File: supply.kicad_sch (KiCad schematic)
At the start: 95 parts, among them J12 Molex_Nano-Fit-105430_xx02-ho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, Q11 PJE138K, Q13 BCM857BS-7-F, Q14 BCM857BS-7-F, Q15 SSM3J332R, Q16 SSM3J332R, Q18 SSM3J332R, Q5 PJE138K, Q6 SSM3J332R, Q7 PJE138K, Q8 PJE138K, SW1 PCM12SMTR, U1 TPS56C230, U29 TPS56C230, U37 74LVC2G14GV, U38 74LVC1G175GV, U41 NCP730BMT330TBG, U42 TPS7A0518PDBVT

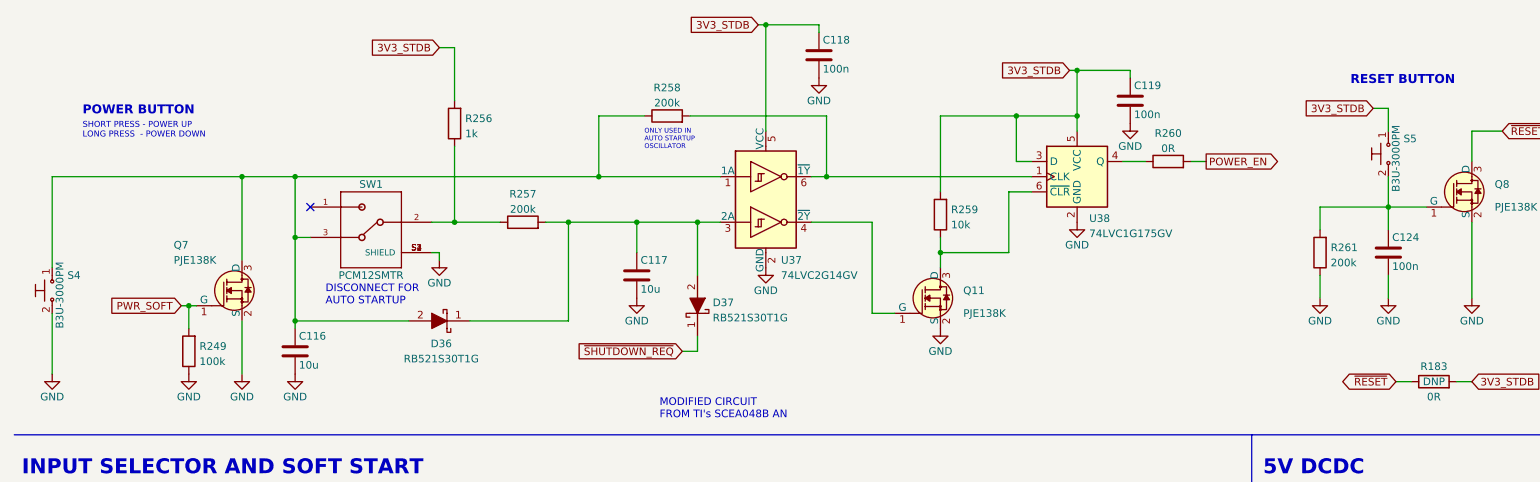
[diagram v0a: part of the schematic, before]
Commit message: Replace buttons with top-actuated ones
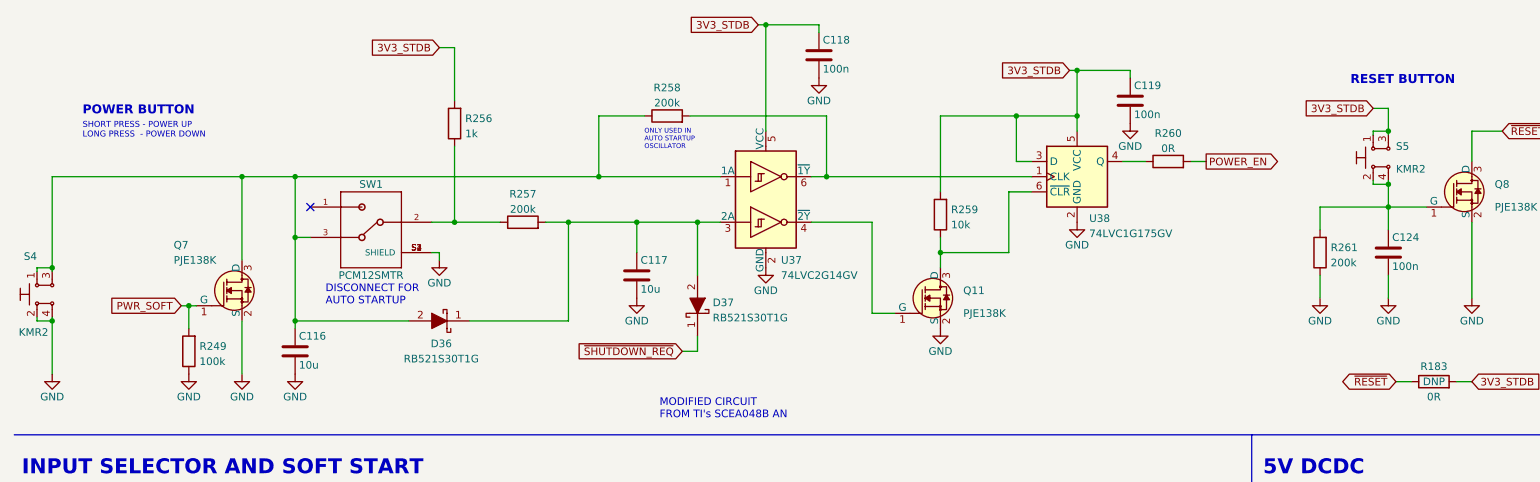
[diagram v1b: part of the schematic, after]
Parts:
- removed S4, S5: B3U-3000PM, jetson-orin-baseboard-footprints:B3U-3000P, symbol jetson-orin-baseboard:B3U-3000PM
- added S4, S5: KMR2, antmicro-footprints:SW_SPST_4.2x2.8, symbol antmicroPushbuttonSwitches:KMR2
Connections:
- net 3V3_STDB: now also S5.1, S5.3
- net GND: now also S4.2, S4.4
- net at C116.1, D36.2, Q7.3 (D)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: now also S4.1, S4.3
- net at C124.1, Q8.1 (G), R261.2: now also S5.2, S5.4
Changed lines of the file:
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@@
   (junction (at 105.41 59.69) (diameter 0) (color 0 0 0 0)
   )
+  (junction (at 19.05 67.31) (diameter 0) (color 0 0 0 0)
+  )
   (junction (at 389.89 199.39) (diameter 0) (color 0 0 0 0)
   )
   (junction (at 81.28 168.91) (diameter 0) (color 0 0 0 0)
   )
+  (junction (at 19.05 76.2) (diameter 0) (color 0 0 0 0)
+  )
   (junction (at 364.49 125.73) (diameter 0) (color 0 0 0 0)
   )
@@
   (junction (at 382.27 30.48) (diameter 0) (color 0 0 0 0)
   )
+  (junction (at 242.57 44.45) (diameter 0) (color 0 0 0 0)
+  )
   (junction (at 375.92 71.12) (diameter 0) (color 0 0 0 0)
   )
@@
   (junction (at 116.84 59.69) (diameter 0) (color 0 0 0 0)
   )
+  (junction (at 242.57 53.34) (diameter 0) (color 0 0 0 0)
+  )
   (junction (at 365.76 125.73) (diameter 0) (color 0 0 0 0)
   )
@@
     (stroke (width 0) (type default) (color 0 0 0 0))
   )
+  (wire (pts (xy 242.57 53.34) (xy 242.57 57.15))
+    (stroke (width 0) (type default) (color 0 0 0 0))
+  )
   (wire (pts (xy 167.64 64.77) (xy 179.07 64.77))
     (stroke (width 0) (type default) (color 0 0 0 0))
@@
     (stroke (width 0) (type default) (color 0 0 0 0))
   )
+  (wire (pts (xy 19.05 75.565) (xy 19.05 76.2))
+    (stroke (width 0) (type default) (color 0 0 0 0))
+  )
   (wire (pts (xy 41.91 73.66) (xy 43.18 73.66))
     (stroke (width 0) (type default) (color 0 0 0 0))
@@
     (stroke (width 0) (type default) (color 0 0 0 0))
   )
+  (wire (pts (xy 242.57 52.705) (xy 242.57 53.34))
+    (stroke (width 0) (type default) (color 0 0 0 0))
+  )
   (wire (pts (xy 86.36 46.99) (xy 86.36 59.69))
     (stroke (width 0) (type default) (color 0 0 0 0))
@@
     (stroke (width 0) (type default) (color 0 0 0 0))
   )
+  (wire (pts (xy 19.05 76.2) (xy 16.51 76.2))
+    (stroke (width 0) (type default) (color 0 0 0 0))
+  )
   (wire (pts (xy 66.04 179.07) (xy 69.85 179.07))
     (stroke (width 0) (type default) (color 0 0 0 0))
@@
     (stroke (width 0) (type default) (color 0 0 0 0))
   )
-  (wire (pts (xy 19.05 74.93) (xy 19.05 85.09))
-    (stroke (width 0) (type default) (color 0 0 0 0))
-  )
   (wire (pts (xy 389.89 198.12) (xy 389.89 199.39))
     (stroke (width 0) (type default) (color 0 0 0 0))
@@
     (stroke (width 0) (type default) (color 0 0 0 0))
   )
+  (wire (pts (xy 19.05 76.2) (xy 19.05 85.09))
+    (stroke (width 0) (type default) (color 0 0 0 0))
+  )
   (wire (pts (xy 125.73 41.91) (xy 148.59 41.91))
     (stroke (width 0) (type default) (color 0 0 0 0))
@@
     (stroke (width 0) (type default) (color 0 0 0 0))
   )
+  (wire (pts (xy 242.57 44.45) (xy 242.57 45.085))
+    (stroke (width 0) (type default) (color 0 0 0 0))
+  )
   (wire (pts (xy 307.34 80.01) (xy 307.34 81.28))
     (stroke (width 0) (type default) (color 0 0 0 0))
@@
     (stroke (width 0) (type default) (color 0 0 0 0))
   )
+  (wire (pts (xy 16.51 76.2) (xy 16.51 75.565))
+    (stroke (width 0) (type default) (color 0 0 0 0))
+  )
   (wire (pts (xy 311.15 219.71) (xy 311.15 209.55))
     (stroke (width 0) (type default) (color 0 0 0 0))
@@
     (stroke (width 0) (type default) (color 0 0 0 0))
   )
+  (wire (pts (xy 240.03 44.45) (xy 240.03 45.085))
+    (stroke (width 0) (type default) (color 0 0 0 0))
+  )
   (wire (pts (xy 347.98 40.64) (xy 347.98 41.91))
     (stroke (width 0) (type default) (color 0 0 0 0))
@@
     (stroke (width 0) (type default) (color 0 0 0 0))
   )
+  (wire (pts (xy 19.05 67.31) (xy 19.05 67.945))
+    (stroke (width 0) (type default) (color 0 0 0 0))
+  )
   (wire (pts (xy 88.9 76.2) (xy 105.41 76.2))
     (stroke (width 0) (type default) (color 0 0 0 0))
@@
     (stroke (width 0) (type default) (color 0 0 0 0))
   )
+  (wire (pts (xy 240.03 53.34) (xy 240.03 52.705))
+    (stroke (width 0) (type default) (color 0 0 0 0))
+  )
   (polyline (pts (xy 289.56 50.8) (xy 407.67 50.8))
     (stroke (width 0) (type default) (color 0 0 0 0))
   )
+  (wire (pts (xy 19.05 67.31) (xy 16.51 67.31))
+    (stroke (width 0) (type default) (color 0 0 0 0))
+  )
   (wire (pts (xy 330.2 30.48) (xy 330.2 33.02))
     (stroke (width 0) (type default) (color 0 0 0 0))
@@
     (stroke (width 0) (type default) (color 0 0 0 0))
   )
-  (wire (pts (xy 337.82 199.39) (xy 342.9 199.39))
+  (wire (pts (xy 16.51 67.31) (xy 16.51 67.945))
     (stroke (width 0) (type default) (color 0 0 0 0))
   )
-  (wire (pts (xy 198.12 49.53) (xy 201.93 49.53))
+  (wire (pts (xy 337.82 199.39) (xy 342.9 199.39))
     (stroke (width 0) (type default) (color 0 0 0 0))
   )
-  (wire (pts (xy 242.57 52.07) (xy 242.57 57.15))
+  (wire (pts (xy 198.12 49.53) (xy 201.93 49.53))
     (stroke (width 0) (type default) (color 0 0 0 0))
   )
@@
     (stroke (width 0) (type default) (color 0 0 0 0))
   )
+  (wire (pts (xy 242.57 53.34) (xy 240.03 53.34))
+    (stroke (width 0) (type default) (color 0 0 0 0))
+  )
   (wire (pts (xy 110.49 41.91) (xy 110.49 52.07))
     (stroke (width 0) (type default) (color 0 0 0 0))
@@
     (stroke (width 0) (type default) (color 0 0 0 0))
   )
+  (wire (pts (xy 242.57 44.45) (xy 240.03 44.45))
+    (stroke (width 0) (type default) (color 0 0 0 0))
+  )
   (wire (pts (xy 365.76 71.12) (xy 375.92 71.12))
     (stroke (width 0) (type default) (color 0 0 0 0))
@@
     (pin "2")
   )
-  (symbol (lib_id "jetson-orin-baseboard:B3U-3000PM") (at 19.05 71.12 90) (mirror x) (unit 1)
-    (in_bom yes) (on_board yes)
-    (property "Reference" "S4" (id 0) (at 21.59 68.58 90)
-      (effects (font (size 1.27 1.27)) (justify right))
-    )
-    (property "Value" "B3U-3000PM" (id 1) (at 20.32 77.47 0)
-      (effects (font (size 1.27 1.27)) (justify right))
-    )
-    (property "Footprint" "jetson-orin-baseboard-footprints:B3U-3000P" (id 2) (at 13.97 76.2 0)
-      (effects (font (size 1.27 1.27)) (justify left) hide)
-    )
-    (property "Datasheet" "http://www.farnell.com/datasheets/2610940.pdf" (id 3) (at 11.43 76.2 0)
-      (effects (font (size 1.524 1.524)) (justify left) hide)
-    )
-    (property "MPN" "B3U-3000PM" (id 4) (at 9.0678 76.0984 0)
-      (effects (font (size 1.524 1.524)) (justify left) hide)
-    )
-    (property "Manufacturer" "OMRON" (id 5) (at 7.0612 76.2 0)
-      (effects (font (size 1.524 1.524)) (justify left) hide)
-    )
-    (pin "1")
-    (pin "2")
-  )
   (symbol (lib_id "jetson-orin-baseboard:R_10k_0402") (at 167.64 135.89 90) (unit 1)
     (in_bom yes) (on_board yes) (fields_autoplaced)
@@
     (pin "2")
   )
+  (symbol (lib_id "antmicroPushbuttonSwitches:KMR2") (at 16.51 71.755 90) (mirror x) (unit 1)
+    (in_bom yes) (on_board yes)
+    (property "Reference" "S4" (id 0) (at 16.51 65.405 90)
+      (effects (font (size 1.27 1.27)) (justify left))
+    )
+    (property "Value" "KMR2" (id 1) (at 18.415 78.105 90)
+      (effects (font (size 1.27 1.27)) (justify left))
+    )
+    (property "Footprint" "antmicro-footprints:SW_SPST_4.2x2.8" (id 2) (at 11.43 76.835 0)
+      (effects (font (size 1.27 1.27)) (justify left) hide)
+    )
+    (property "Datasheet" "http://www.farnell.com/datasheets/2631211.pdf" (id 3) (at 8.89 76.835 0)
+      (effects (font (size 1.524 1.524)) (justify left) hide)
+    )
+    (property "MPN" "KMR211NGLFS" (id 4) (at 6.5278 76.7334 0)
+      (effects (font (size 1.524 1.524)) (justify left) hide)
+    )
+    (property "Manufacturer" "C&K Components" (id 5) (at 4.5212 76.835 0)
+      (effects (font (size 1.524 1.524)) (justify left) hide)
+    )
+    (pin "1")
+    (pin "2")
+    (pin "3")
+    (pin "4")
+  )
   (symbol (lib_id "jetson-orin-baseboard:LTST-C190GKT") (at 167.64 147.32 270) (unit 1)
     (in_bom yes) (on_board yes)
@@
     (pin "2")
   )
-  (symbol (lib_id "jetson-orin-baseboard:B3U-3000PM") (at 242.57 48.26 90) (mirror x) (unit 1)
-    (in_bom yes) (on_board yes)
-    (property "Reference" "S5" (id 0) (at 245.11 45.72 90)
-      (effects (font (size 1.27 1.27)) (justify right))
-    )
-    (property "Value" "B3U-3000PM" (id 1) (at 243.84 54.61 0)
-      (effects (font (size 1.27 1.27)) (justify right))
-    )
-    (property "Footprint" "jetson-orin-baseboard-footprints:B3U-3000P" (id 2) (at 237.49 53.34 0)
-      (effects (font (size 1.27 1.27)) (justify left) hide)
-    )
-    (property "Datasheet" "http://www.farnell.com/datasheets/2610940.pdf" (id 3) (at 234.95 53.34 0)
-      (effects (font (size 1.524 1.524)) (justify left) hide)
-    )
-    (property "MPN" "B3U-3000PM" (id 4) (at 232.5878 53.2384 0)
-      (effects (font (size 1.524 1.524)) (justify left) hide)
-    )
-    (property "Manufacturer" "OMRON" (id 5) (at 230.5812 53.34 0)
-      (effects (font (size 1.524 1.524)) (justify left) hide)
-    )
-    (pin "1")
-    (pin "2")
-  )
   (symbol (lib_id "jetson-orin-baseboard:R_10k_0402") (at 81.28 151.13 90) (unit 1)
     (in_bom yes) (on_board yes) (fields_autoplaced)
@@
     (pin "5")
   )
+  (symbol (lib_id "antmicroPushbuttonSwitches:KMR2") (at 240.03 48.895 90) (mirror x) (unit 1)
+    (in_bom yes) (on_board yes)
+    (property "Reference" "S5" (id 0) (at 243.84 46.99 90)
+      (effects (font (size 1.27 1.27)) (justify right))
+    )
+    (property "Value" "KMR2" (id 1) (at 243.84 50.8 90)
+      (effects (font (size 1.27 1.27)) (justify right))
+    )
+    (property "Footprint" "antmicro-footprints:SW_SPST_4.2x2.8" (id 2) (at 234.95 53.975 0)
+      (effects (font (size 1.27 1.27)) (justify left) hide)
+    )
+    (property "Datasheet" "http://www.farnell.com/datasheets/2631211.pdf" (id 3) (at 232.41 53.975 0)
+      (effects (font (size 1.524 1.524)) (justify left) hide)
+    )
+    (property "MPN" "KMR211NGLFS" (id 4) (at 230.0478 53.8734 0)
+      (effects (font (size 1.524 1.524)) (justify left) hide)
+    )
+    (property "Manufacturer" "C&K Components" (id 5) (at 228.0412 53.975 0)
+      (effects (font (size 1.524 1.524)) (justify left) hide)
+    )
+    (pin "1")
+    (pin "2")
+    (pin "3")
+    (pin "4")
+  )
   (symbol (lib_id "antmicroResistors0603:R_0R_0603_HPWR") (at 382.27 199.39 0) (unit 1)

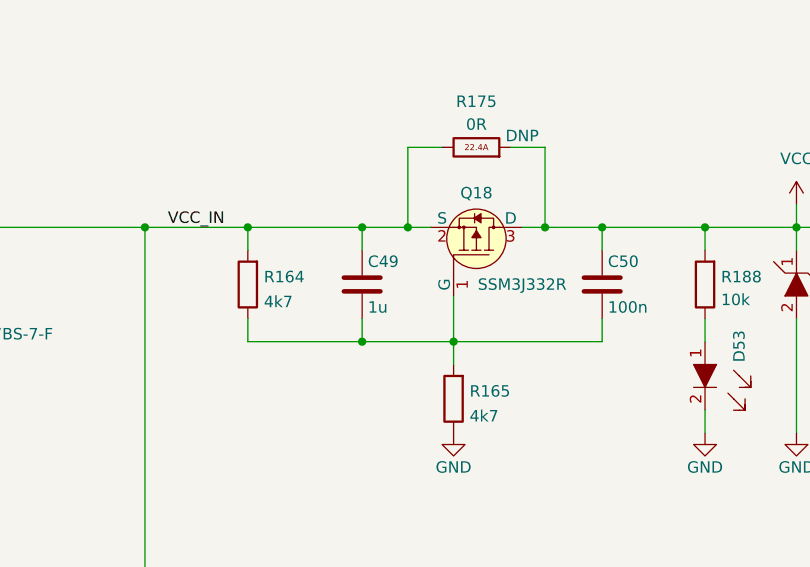
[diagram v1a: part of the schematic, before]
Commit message: Replace 1u/10V cap with 1u/25V one
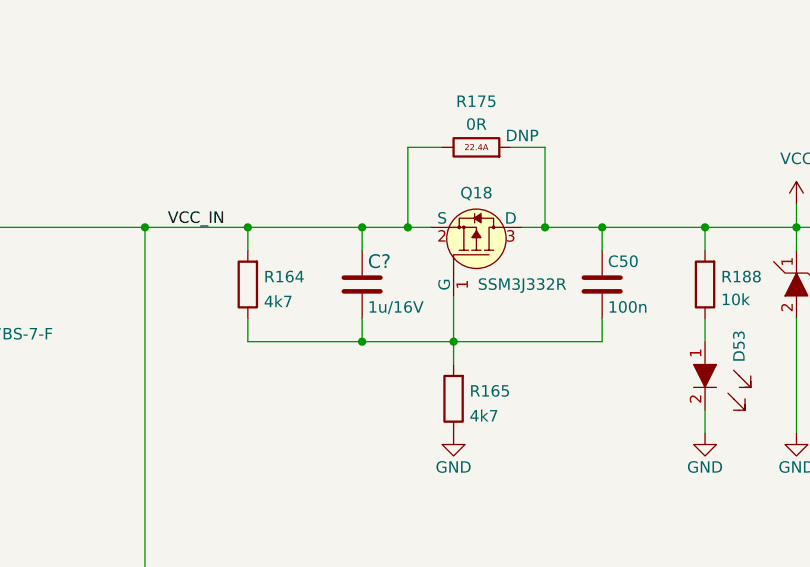
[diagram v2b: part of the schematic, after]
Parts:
- removed C49: C_1u_0402, jetson-orin-baseboard-footprints:0402-cap, symbol jetson-orin-baseboard:C_1u_0402
- added C?: C_1u_0402_16V, antmicro-footprints:0402-cap, symbol antmicroCapacitors0402:C_1u_0402_16V
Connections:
- net VCC_IN: now also C?.1
- net at C50.2, Q18.1 (G), R164.1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: now also C?.2
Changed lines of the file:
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@@
+    (pin "2")
+  )
+  (symbol (lib_id "antmicroCapacitors0402:C_1u_0402_16V") (at 129.54 135.89 0) (unit 1)
+    (in_bom yes) (on_board yes)
+    (property "Reference" "C?" (id 0) (at 130.175 133.35 0)
+      (effects (font (size 1.524 1.524)) (justify left))
+    )
+    (property "Value" "C_1u_0402_16V" (id 1) (at 129.54 139.7 0)
+      (effects (font (size 1.524 1.524)) hide)
+    )
+    (property "Footprint" "antmicro-footprints:0402-cap" (id 2) (at 134.62 130.81 0)
+      (effects (font (size 1.524 1.524)) (justify left) hide)
+    )
+    (property "Datasheet" "" (id 3) (at 129.54 135.89 0)
+      (effects (font (size 1.27 1.27)) hide)
+    )
+    (property "Manufacturer" "Kemet" (id 4) (at 134.62 125.73 0)
+      (effects (font (size 1.524 1.524)) (justify left) hide)
+    )
+    (property "MPN" "C0402C105M4PACTU" (id 5) (at 134.62 128.27 0)
+      (effects (font (size 1.524 1.524)) (justify left) hide)
+    )
+    (property "Val" "1u/16V" (id 6) (at 130.175 138.43 0)
+      (effects (font (size 1.27 1.27)) (justify left))
+    )
+    (pin "1")
     (pin "2")
   )
@@
     (pin "1")
   )
-  (symbol (lib_id "jetson-orin-baseboard:C_1u_0402") (at 129.54 135.89 0) (unit 1)
-    (in_bom yes) (on_board yes)
-    (property "Reference" "C49" (id 0) (at 130.175 133.35 0)
-      (effects (font (size 1.27 1.27)) (justify left))
-    )
-    (property "Value" "C_1u_0402" (id 1) (at 129.54 139.7 0)
-      (effects (font (size 1.27 1.27)) hide)
-    )
-    (property "Footprint" "jetson-orin-baseboard-footprints:0402-cap" (id 2) (at 134.62 130.81 0)
-      (effects (font (size 1.524 1.524)) (justify left) hide)
-    )
-    (property "Datasheet" "" (id 3) (at 129.54 135.89 0)
-      (effects (font (size 1.27 1.27)) hide)
-    )
-    (property "Manufacturer" "TDK" (id 4) (at 134.62 125.73 0)
-      (effects (font (size 1.524 1.524)) (justify left) hide)
-    )
-    (property "MPN" "C1005X6S1A105K050BC" (id 5) (at 134.62 128.27 0)
-      (effects (font (size 1.524 1.524)) (justify left) hide)
-    )
-    (property "Val" "1u" (id 6) (at 130.175 138.43 0)
-      (effects (font (size 1.27 1.27)) (justify left))
-    )
-    (pin "1")
-    (pin "2")
-  )
   (symbol (lib_id "jetson-orin-baseboard:C_1u_0402") (at 280.67 217.17 0) (unit 1)

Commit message: Add resistor to slow down discharge of U37 2A input. Add TVS to S4 and S5
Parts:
- added D? (x2): TPD1E0B04DPYR, jetson-orin-baseboard-footprints:XDFN-2_1x0.60mm, symbol jetson-orin-baseboard:TPD1E0B04DPYR
- added R?: R_200R_0402, jetson-orin-baseboard-footprints:0402-res, symbol jetson-orin-baseboard:R_200R_0402
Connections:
- net GND: now also D?.1, D?.1
- net ~{SHUTDOWN_REQ}: now also R?.2; no longer D37.1
- net at C116.1, D36.2, Q7.3 (D)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: now also D?.2
- net at C124.1, Q8.1 (G), R261.2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: now also D?.2
- new net: D37.1, R?.1
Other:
- moved on the sheet: C116, C117, D36, Q11, Q7, R249, R256, R257, R259, S4

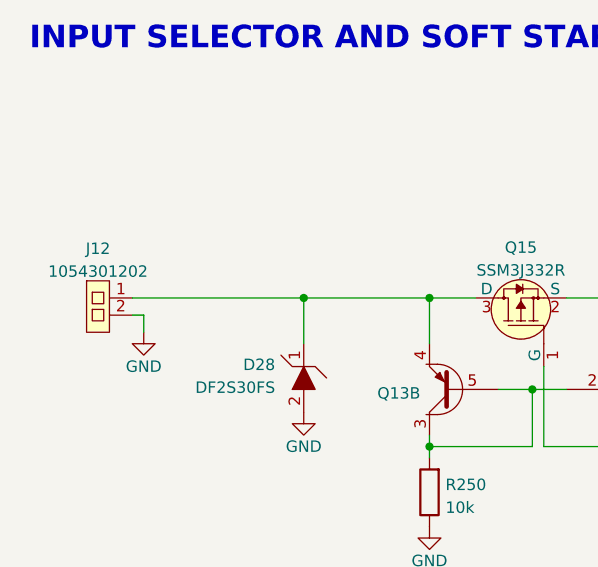
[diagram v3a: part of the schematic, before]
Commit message: Add input voltage info near J12 (DC connector)
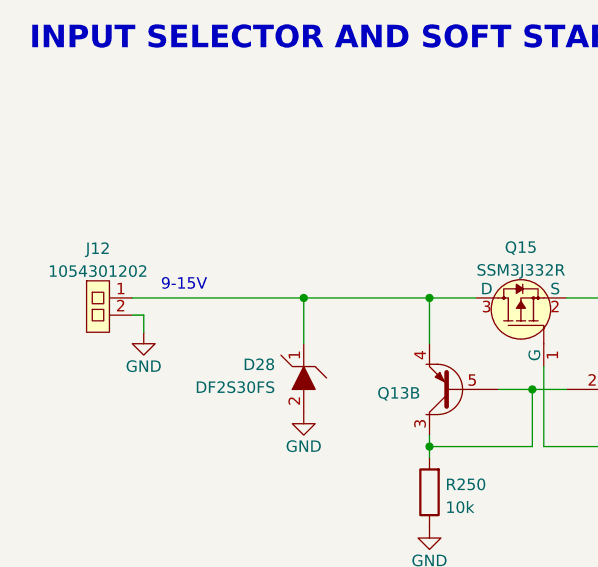
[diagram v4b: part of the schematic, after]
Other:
- note added: "9-15V"
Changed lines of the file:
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@@
+    (effects (font (size 1.27 1.27)) (justify left bottom))
+  )
+  (text "9-15V " (at 28.575 128.905 0)
     (effects (font (size 1.27 1.27)) (justify left bottom))
   )
